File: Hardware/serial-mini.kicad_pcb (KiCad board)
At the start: 4 copper layers, 97 x 42 mm, 82 parts, among them J1 PICKIT V3 Header, J2 10103593-0001LF, J3 Serial Port, Q1 IRLML2060, Q2 IRLML2060, Q3 IRLML2060, U1 MAX232, U2 SN74AHC14RGYR, U3 DSPIC33CK64MP102, U4 MIC5504-3.3YM5-TR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

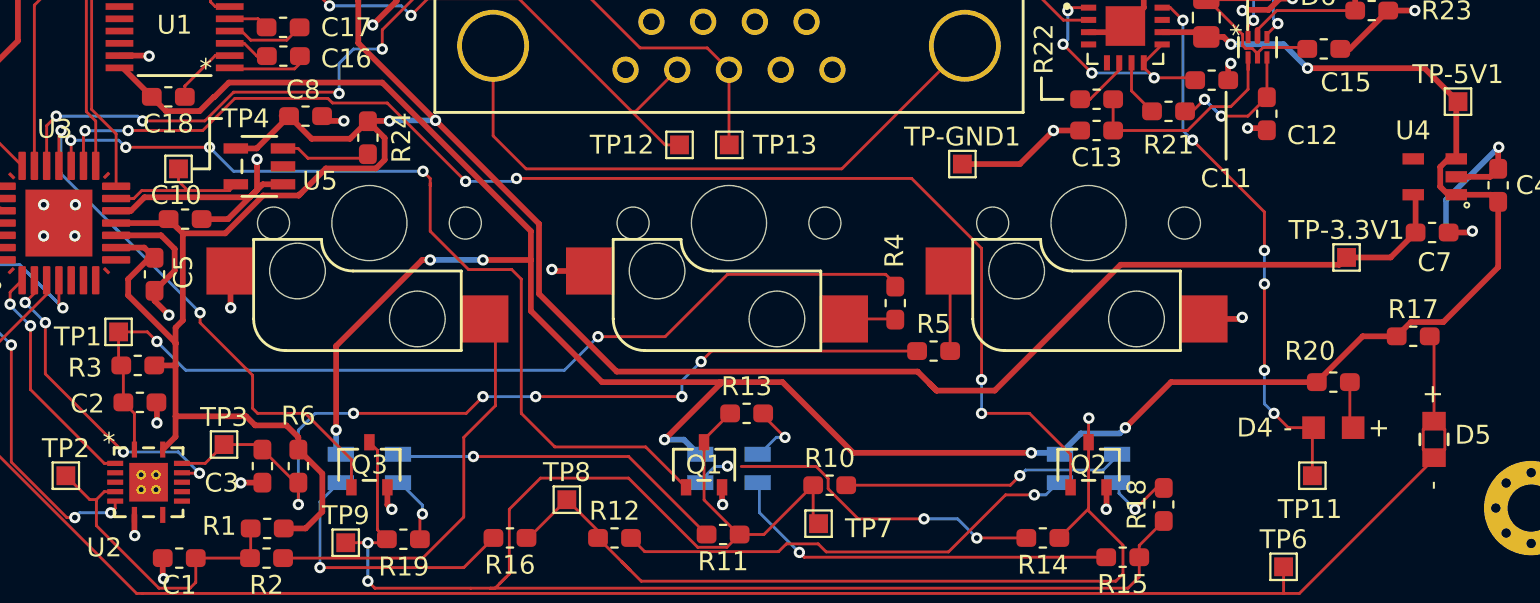
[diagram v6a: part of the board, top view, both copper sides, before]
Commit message: Add 3D file references
Generated first build
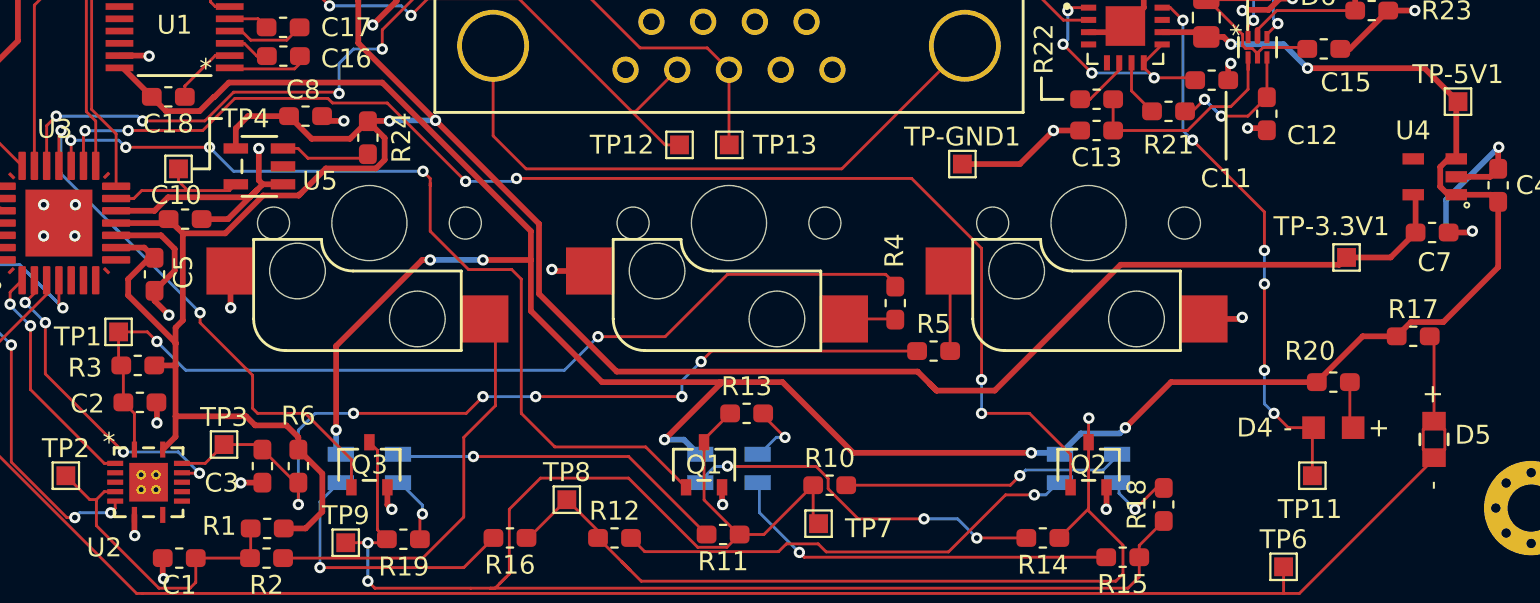
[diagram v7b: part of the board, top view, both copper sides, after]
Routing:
- net Net-(D2-Pad1): track 18.9 -> 19.6 mm
- net +3V3: track 195.9 -> 196.5 mm
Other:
- board text added: "By Chris Bell"
- board text added: "Serial Mini Keyboard"
